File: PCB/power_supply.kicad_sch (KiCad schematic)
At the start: 22 parts

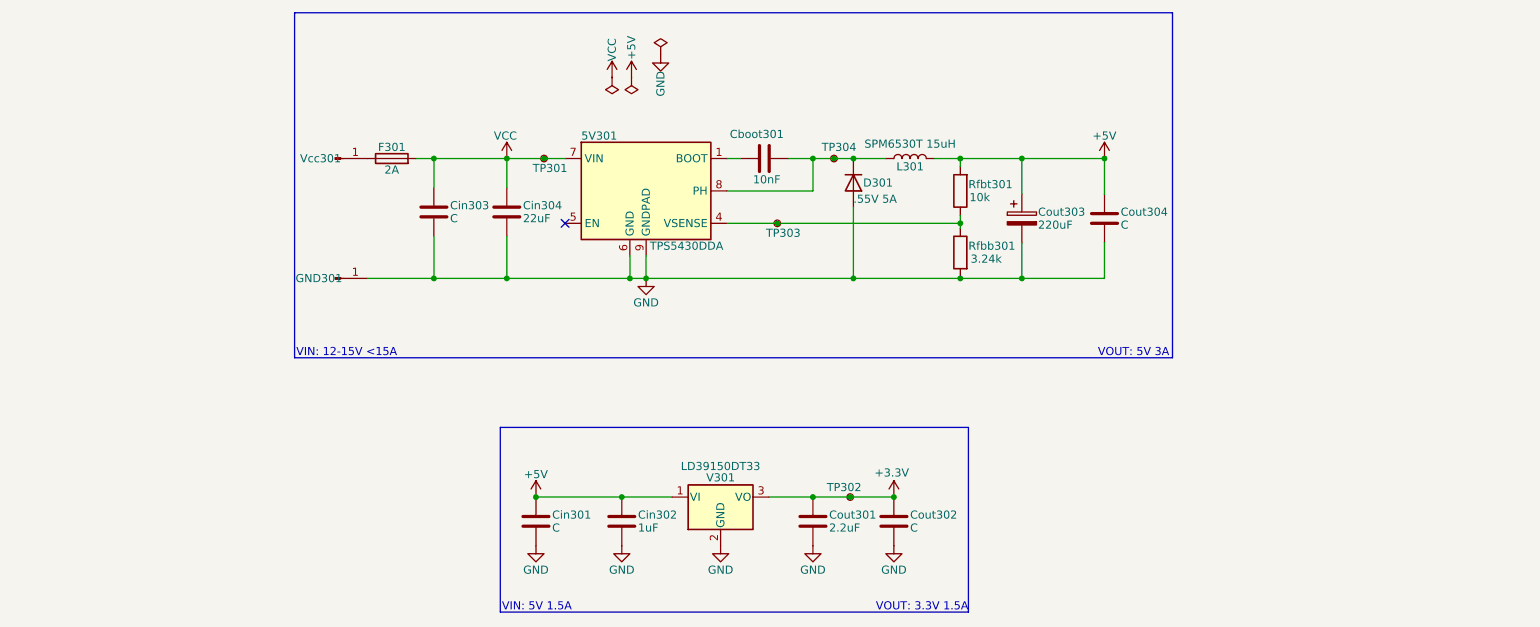
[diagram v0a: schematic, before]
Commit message: Applied recommendations from my coworker; Fixed badly placed filter caps; Added flyback diode to fan circuit; Applied larger grid and some spacing to the schematics; And some other small adjustments
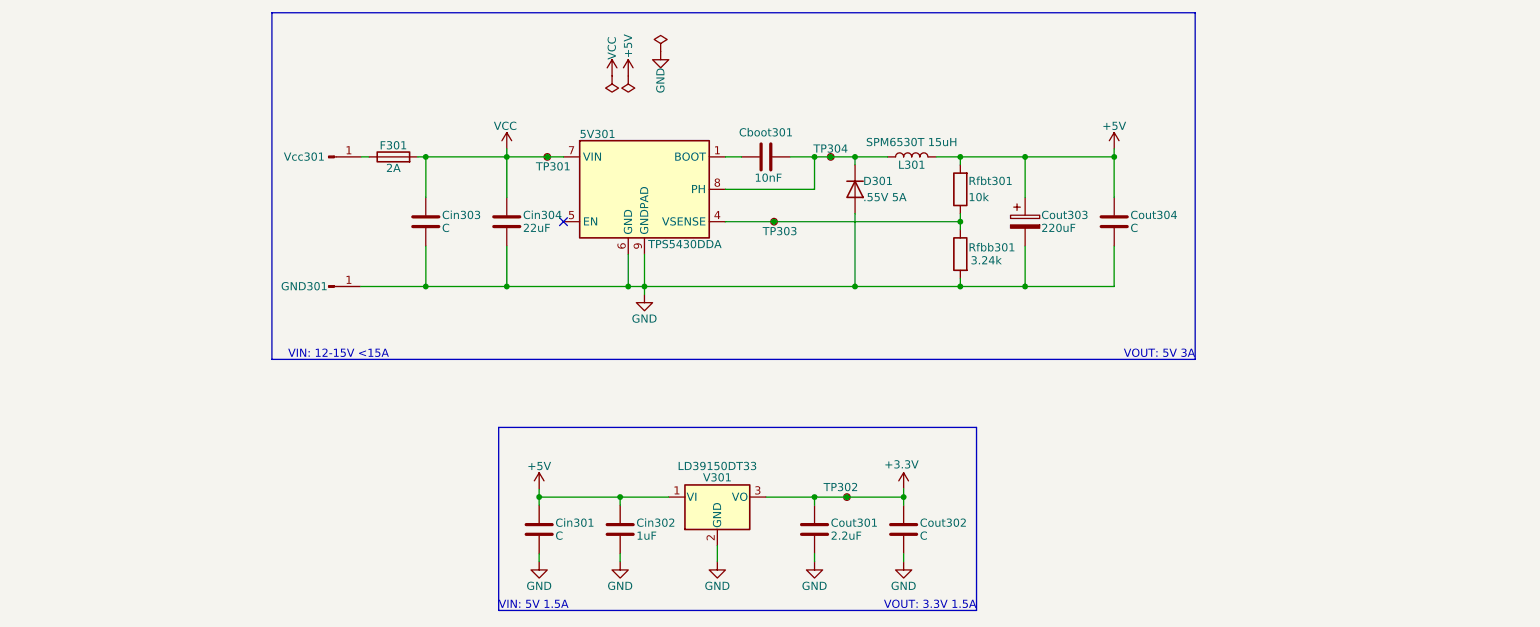
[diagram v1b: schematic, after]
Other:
- title: (none) -> Power Supplies
- moved on the sheet: Cin301, Cin302, Cin303, Cin304, Cout301, Cout302, Cout303, Cout304, D301, GND301, TP301, TP302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

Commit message: Changed some resistor and capacitor values;Added additional input electrolytic cap;Selected LCSC parts;Added diode footprint;Removed 3.3V power supply and decreased the output of the 5V supply to 3.3V;Added flyback diode on the fan circuit;Added LDO between the USB-C VBUS and the 5V rail
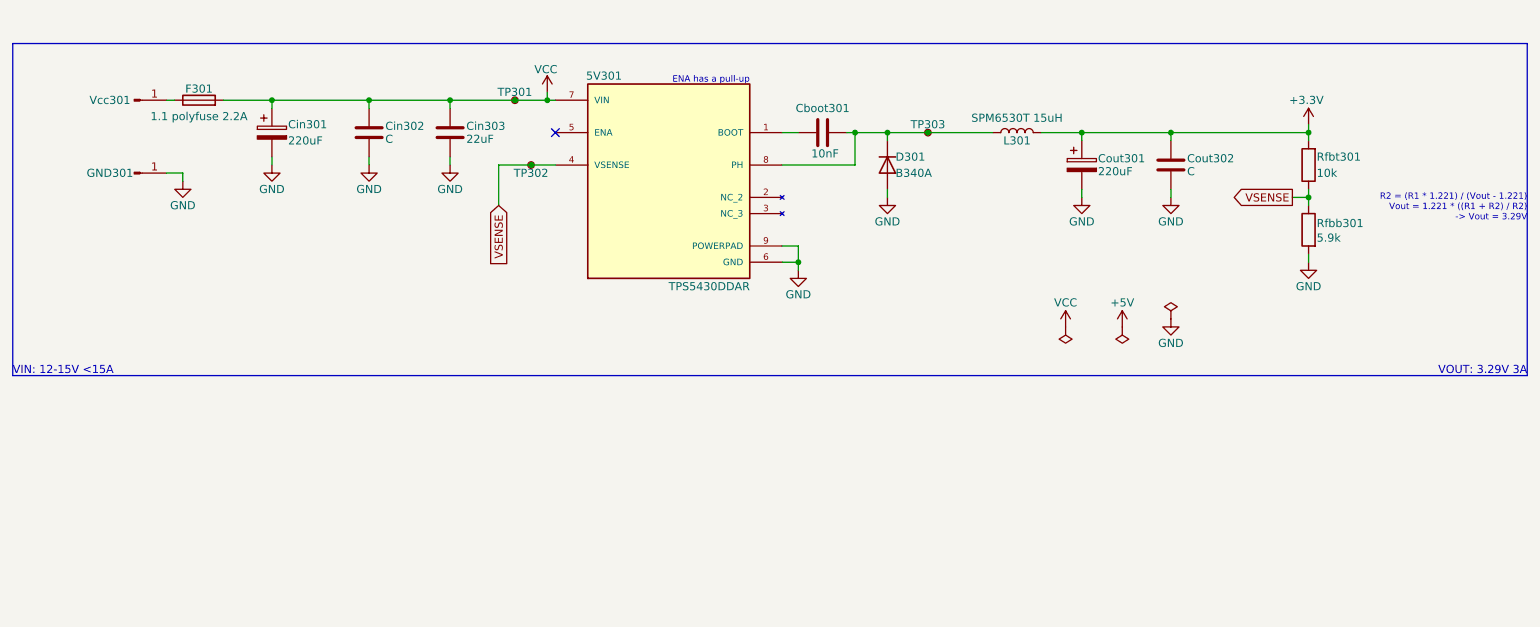
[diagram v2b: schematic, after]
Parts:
- removed 5V301: TPS5430DDA, Package_SO:TI_SO-PowerPAD-8_ThermalVias, symbol Regulator_Switching:TPS5430DDA
- removed Cin301, Cout302: C, Capacitor_SMD:C_0805_2012Metric, symbol Device:C
- removed Cin302: 1uF, Capacitor_SMD:C_0805_2012Metric, symbol Device:C
- removed Cout301: 2.2uF, Capacitor_SMD:C_0805_2012Metric, symbol Device:C
- removed TP302: TestPoint_Small, TestPoint:TestPoint_Pad_D1.0mm, symbol Connector:TestPoint_Small
- removed V301: LD39150DT33, Package_TO_SOT_SMD:TO-252-3_TabPin2, symbol Regulator_Linear:LD39150DT33
- added 5V301: TPS5430DDAR, TPS5430DDAR:CONV_TPS5430DDAR, symbol TPS5430DDAR:TPS5430DDAR
- added Cin301: 220uF, Capacitor_SMD:CP_Elec_6.3x7.7, symbol Device:C_Polarized
- D301: value .55V 5A -> B340A
- F301: value 2A -> 1.1 polyfuse 2.2A
- GND301: now left out of the parts list
- Rfbb301: value 3.24k -> 5.9k
- renumbered Cin303 to Cin302, Cin304 to Cin303, Cout303 to Cout301, Cout304 to Cout302, TP303 to TP302, TP304 to TP303
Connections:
- net +3.3V: now also Cout301.1, Cout302.2, L301.2, Rfbt301.2
- net +5V: no longer Cout301.1, Cout302.2, L301.2, Rfbt301.2
- net GND: now also 5V301.6 (GND), 5V301.9 (POWERPAD), Cin301.2
- net VCC: now also 5V301.7 (VIN), Cin301.1
- net at Cboot301.1, D301.1 (K), L301.1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: now also 5V301.8 (PH)
- net at Cboot301.2: now also 5V301.1 (BOOT)
- net VSENSE: now reaches Rfbb301.1, Rfbt301.1, TP302.1
- net VSENSE: now also 5V301.4 (VSENSE)
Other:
- note added: "ENA has a pull-up"
- note added: "R2 = (R1 * 1.221) / (Vout - 1.221) Vout = 1.221 * ((R1 + R2) / R2) -> Vout = 3.29V"
- note added: "VOUT: 3.29V 3A"
- note removed: "VIN: 5V 1.5A"
- note removed: "VOUT: 3.3V 1.5A"
- note removed: "VOUT: 5V 3A"
- title: Power Supplies -> Power Supply
- moved on the sheet: Cboot301, Cin302, Cin303, Cout301, Cout302, D301, F301, GND301, L301, Rfbb301, Rfbt301, TP301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
